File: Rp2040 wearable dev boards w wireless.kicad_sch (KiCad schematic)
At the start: 79 parts, among them IC1 NRF24L01P-R7, J1 battery plug, J2 UJ31-CH-31-SMT-TR, J3 Conn_01x20, J4 Conn_01x20, J5 Conn_01x04, J6 EMPCB.SMAFSTJ.B.HT, Q1 Si2301, SW1 B3U-1100P, SW2 power Switch, U1 MCP73831T-4ADI/OT, U2 W25Q128JVS, U3 TPD4E02B04QDQARQ1, U4 NCP1117-3.3_TO252, U5 RP2040, U6 ADS7830, U7 MPU-6500, Y1 ABLS-12.000MHZ-B4-T, Y2 ECS-160-9-42-CKM-TR

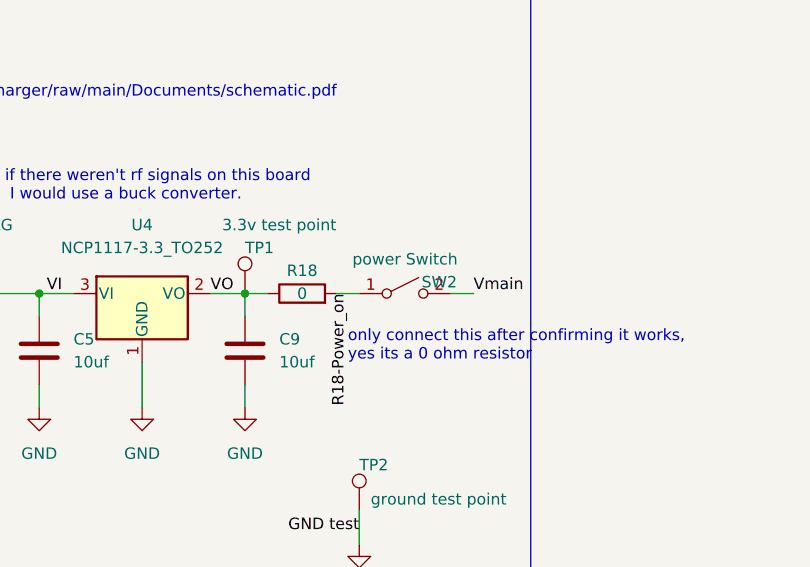
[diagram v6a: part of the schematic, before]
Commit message: routed power
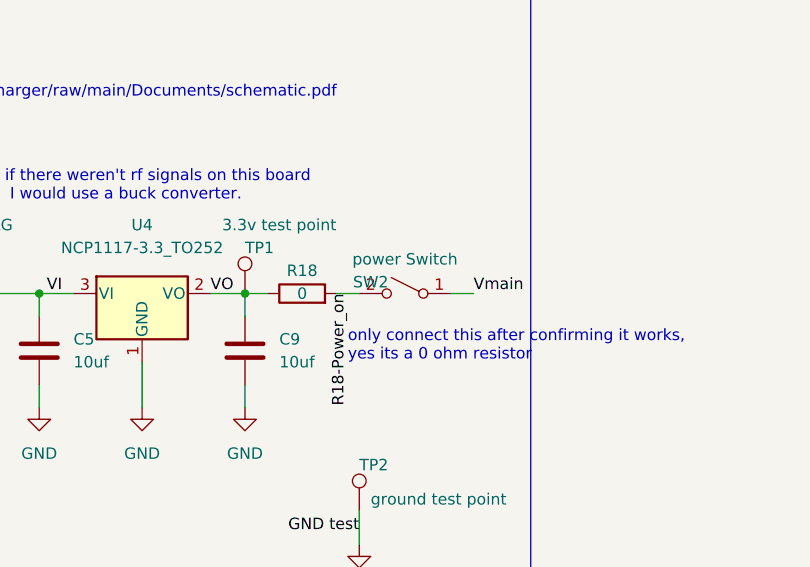
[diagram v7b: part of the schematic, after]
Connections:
- net R18-Power_on: now also SW2.2 (B); no longer SW2.1 (A)
- net Vmain: now also SW2.1 (A); no longer SW2.2 (B)
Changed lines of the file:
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@@
     (pin "1")
   )
-  (symbol (lib_id "Switch:SW_SPST") (at 151.13 114.3 0) (unit 1)
+  (symbol (lib_id "Switch:SW_SPST") (at 151.13 114.3 0) (mirror y) (unit 1)
     (in_bom yes) (on_board yes)
-    (property "Reference" "SW2" (id 0) (at 154.94 113.03 0))
+    (property "Reference" "SW2" (id 0) (at 147.32 113.03 0))
     (property "Value" "power Switch" (id 1) (at 151.13 110.49 0))
     (property "Footprint" "Connector_JST:JST_PH_S2B-PH-SM4-TB_1x02-1MP_P2.00mm_Horizontal" (id 2) (at 151.13 114.3 0)

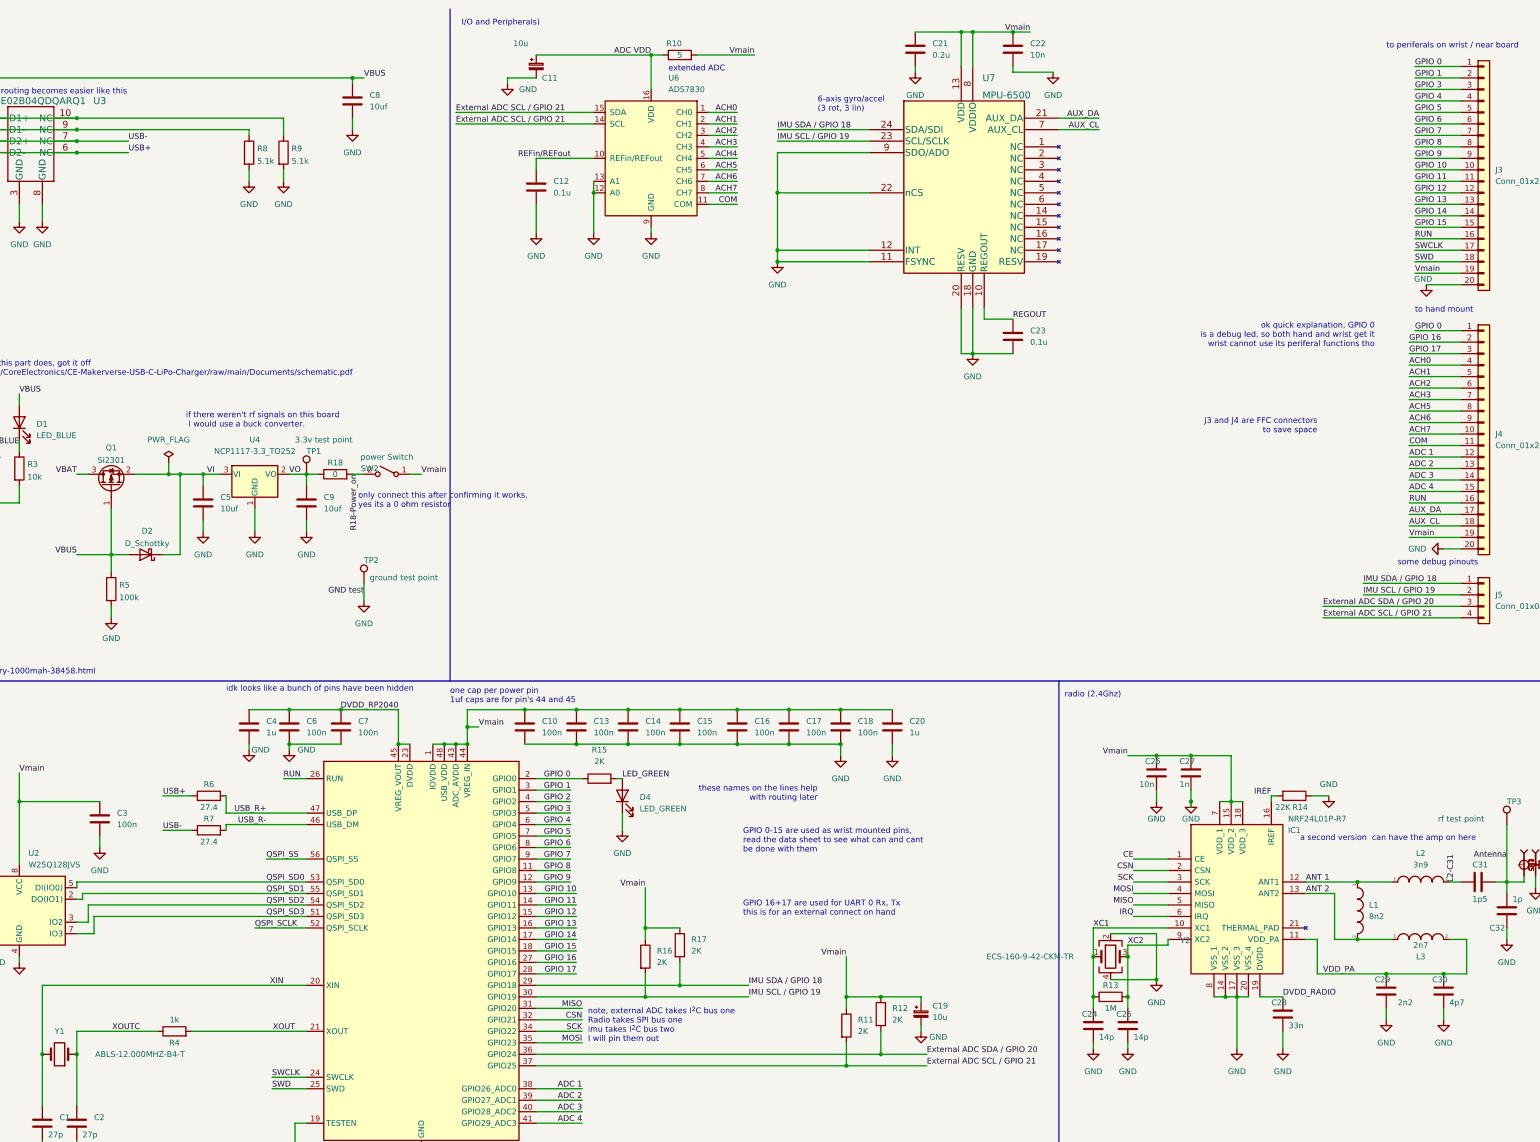
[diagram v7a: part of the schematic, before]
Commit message: started pinning out Rp2040 shortened board to 60 something long
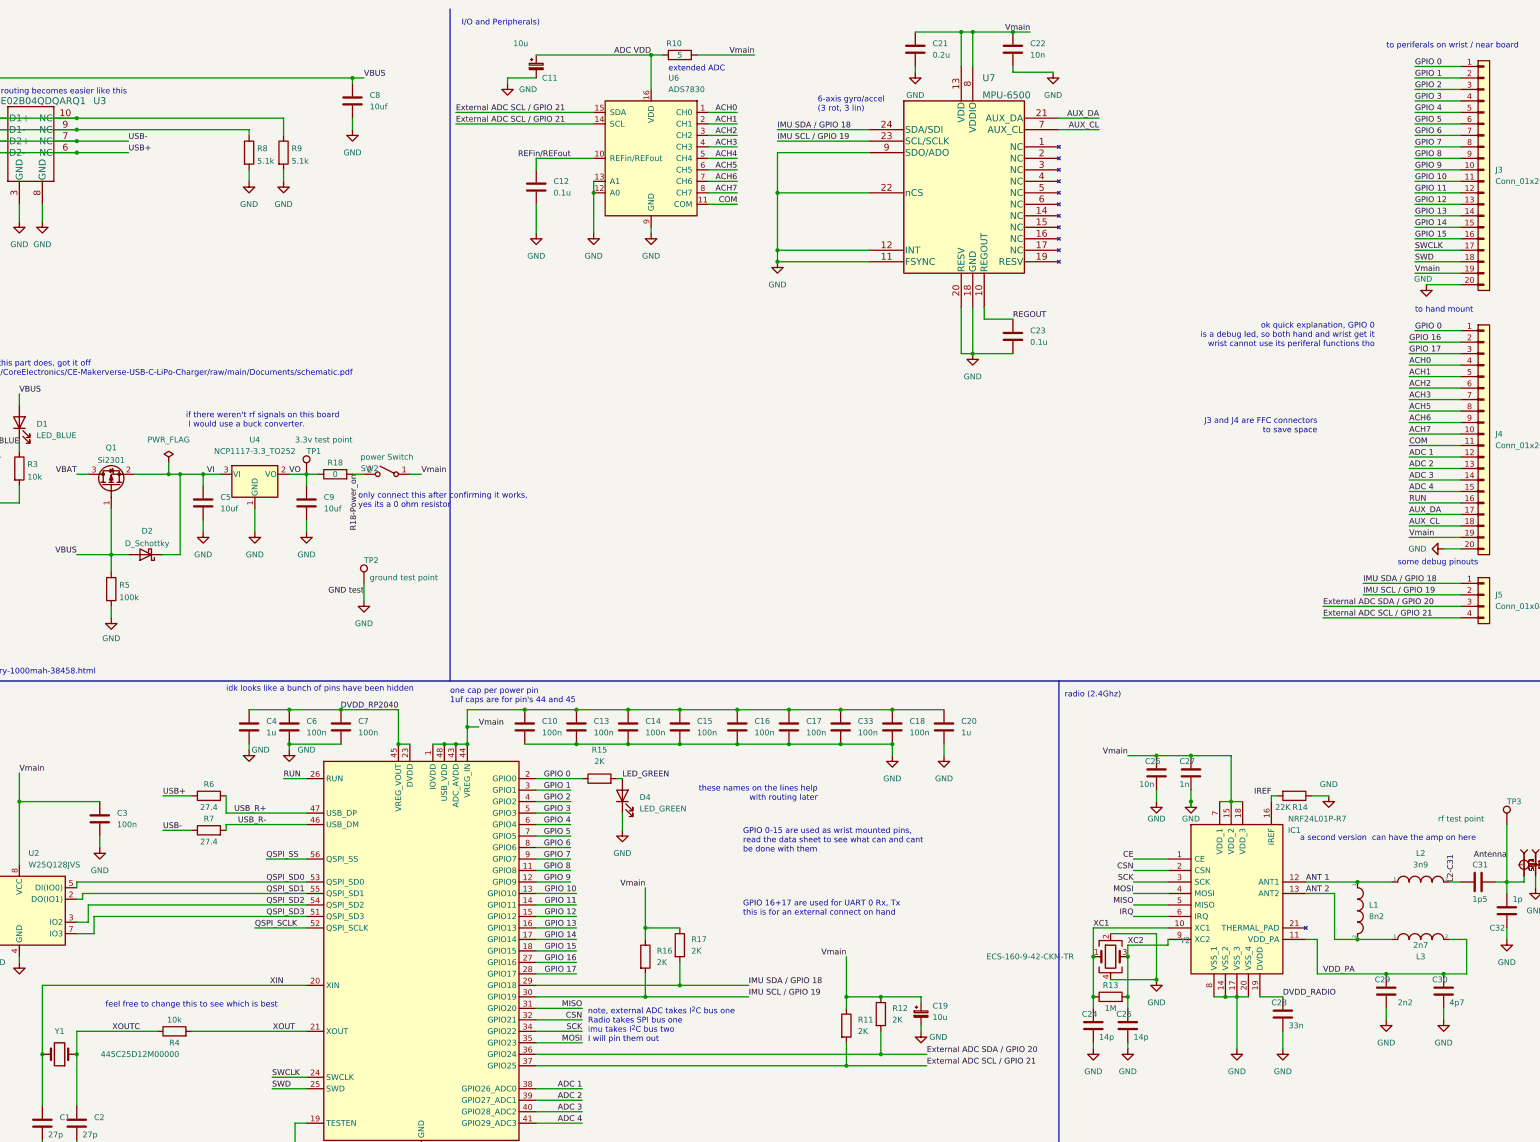
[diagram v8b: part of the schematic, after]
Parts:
- added C33: 100n, Capacitor_SMD:C_01005_0402Metric, symbol Device:C
- R4: value 1k -> 10k
- Y1: value ABLS-12.000MHZ-B4-T -> 445C25D12M00000; footprint ABLS-12:ABLS-12.000MHZ-B4-T -> Crystal:Crystal_SMD_5032-2Pin_5.0x3.2mm_HandSoldering
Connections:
- net GND: now also C33.2
- net GPIO 10: now also J3.11 (Pin_11); no longer J3.10 (Pin_10)
- net GPIO 11: now also J3.12 (Pin_12); no longer J3.11 (Pin_11)
- net GPIO 12: now also J3.13 (Pin_13); no longer J3.12 (Pin_12)
- net GPIO 13: now also J3.14 (Pin_14); no longer J3.13 (Pin_13)
- net GPIO 14: now also J3.15 (Pin_15); no longer J3.14 (Pin_14)
- net GPIO 15: now also J3.16 (Pin_16); no longer J3.15 (Pin_15)
- net GPIO 2: now also J3.3 (Pin_3)
- net GPIO 3: now also J3.4 (Pin_4); no longer J3.3 (Pin_3)
- net GPIO 4: now also J3.5 (Pin_5); no longer J3.4 (Pin_4)
- net GPIO 5: now also J3.6 (Pin_6); no longer J3.5 (Pin_5)
- net GPIO 6: now also J3.7 (Pin_7); no longer J3.6 (Pin_6)
- net GPIO 7: now also J3.8 (Pin_8); no longer J3.7 (Pin_7)
- net GPIO 8: now also J3.9 (Pin_9); no longer J3.8 (Pin_8)
- net GPIO 9: now also J3.10 (Pin_10); no longer J3.9 (Pin_9)
- net RUN: no longer J3.16 (Pin_16)
- net Vmain: now also C33.1
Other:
- note added: "feel free to change this to see which is best"
- moved on the sheet: C18, C20
